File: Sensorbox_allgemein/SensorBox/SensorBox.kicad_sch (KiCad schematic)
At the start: 29 parts, among them J1 SD_Card, Q1 NPN, U2 PS1-O3-100, U3 Beetle ESP32-C6, U5 HPP845E131R5, U6 TPS629211QDRLRQ1

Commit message: code
änderung
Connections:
- net 1.8+: no longer C1.1, C2.1, HM2.2 (CSB), HM2.6 (VDDIO), HM2.8 (VDD)
- net VDD_3V3: now also C1.1, C2.1, HM2.2 (CSB), HM2.6 (VDDIO), HM2.8 (VDD)

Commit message: dee
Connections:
- net 1.8+ is gone; now on net VDD_3V3: R1.2, R2.2
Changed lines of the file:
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@@
+	(wire
+		(pts
+			(xy 157.48 116.84) (xy 158.75 116.84)
+		)
+		(stroke
+			(width 0)
+			(type default)
+		)
+	)
 	(wire
 		(pts
@@
 		(pts
 			(xy 219.71 114.3) (xy 255.27 114.3)
+		)
+		(stroke
+			(width 0)
+			(type default)
+		)
+	)
+	(wire
+		(pts
+			(xy 175.26 116.84) (xy 176.53 116.84)
 		)
 		(stroke
@@
 		)
 	)
-	(global_label "1.8+"
-		(shape input)
-		(at 157.48 116.84 0)
-		(fields_autoplaced yes)
-		(effects
-			(font
-				(size 1.27 1.27)
-			)
-			(justify left)
-		)
-		(property "Intersheetrefs" "${INTERSHEET_REFS}"
-			(at 165.0614 116.84 0)
-			(effects
-				(font
-					(size 1.27 1.27)
-				)
-				(justify left)
-				(hide yes)
-			)
-		)
-	)
 	(global_label "SCL_GPIO20"
 		(shape input)
@@
 		)
 	)
-	(global_label "1.8+"
-		(shape input)
-		(at 175.26 116.84 0)
-		(fields_autoplaced yes)
-		(effects
-			(font
-				(size 1.27 1.27)
-			)
-			(justify left)
-		)
-		(property "Intersheetrefs" "${INTERSHEET_REFS}"
-			(at 182.8414 116.84 0)
+	(global_label "VDD_3V3"
+		(shape input)
+		(at 158.75 116.84 0)
+		(fields_autoplaced yes)
+		(effects
+			(font
+				(size 1.27 1.27)
+			)
+			(justify left)
+		)
+		(property "Intersheetrefs" "${INTERSHEET_REFS}"
+			(at 169.839 116.84 0)
 			(effects
 				(font
@@
 				(hide yes)
 			)
+		)
+	)
+	(global_label "VDD_3V3"
+		(shape input)
+		(at 176.53 116.84 0)
+		(fields_autoplaced yes)
+		(effects
+			(font
+				(size 1.27 1.27)
+			)
+			(justify left)
+		)
+		(property "Intersheetrefs" "${INTERSHEET_REFS}"
+			(at 187.619 116.84 0)
+			(effects
+				(font
+					(size 1.27 1.27)
+				)
+				(justify left)
+				(hide yes)
+			)

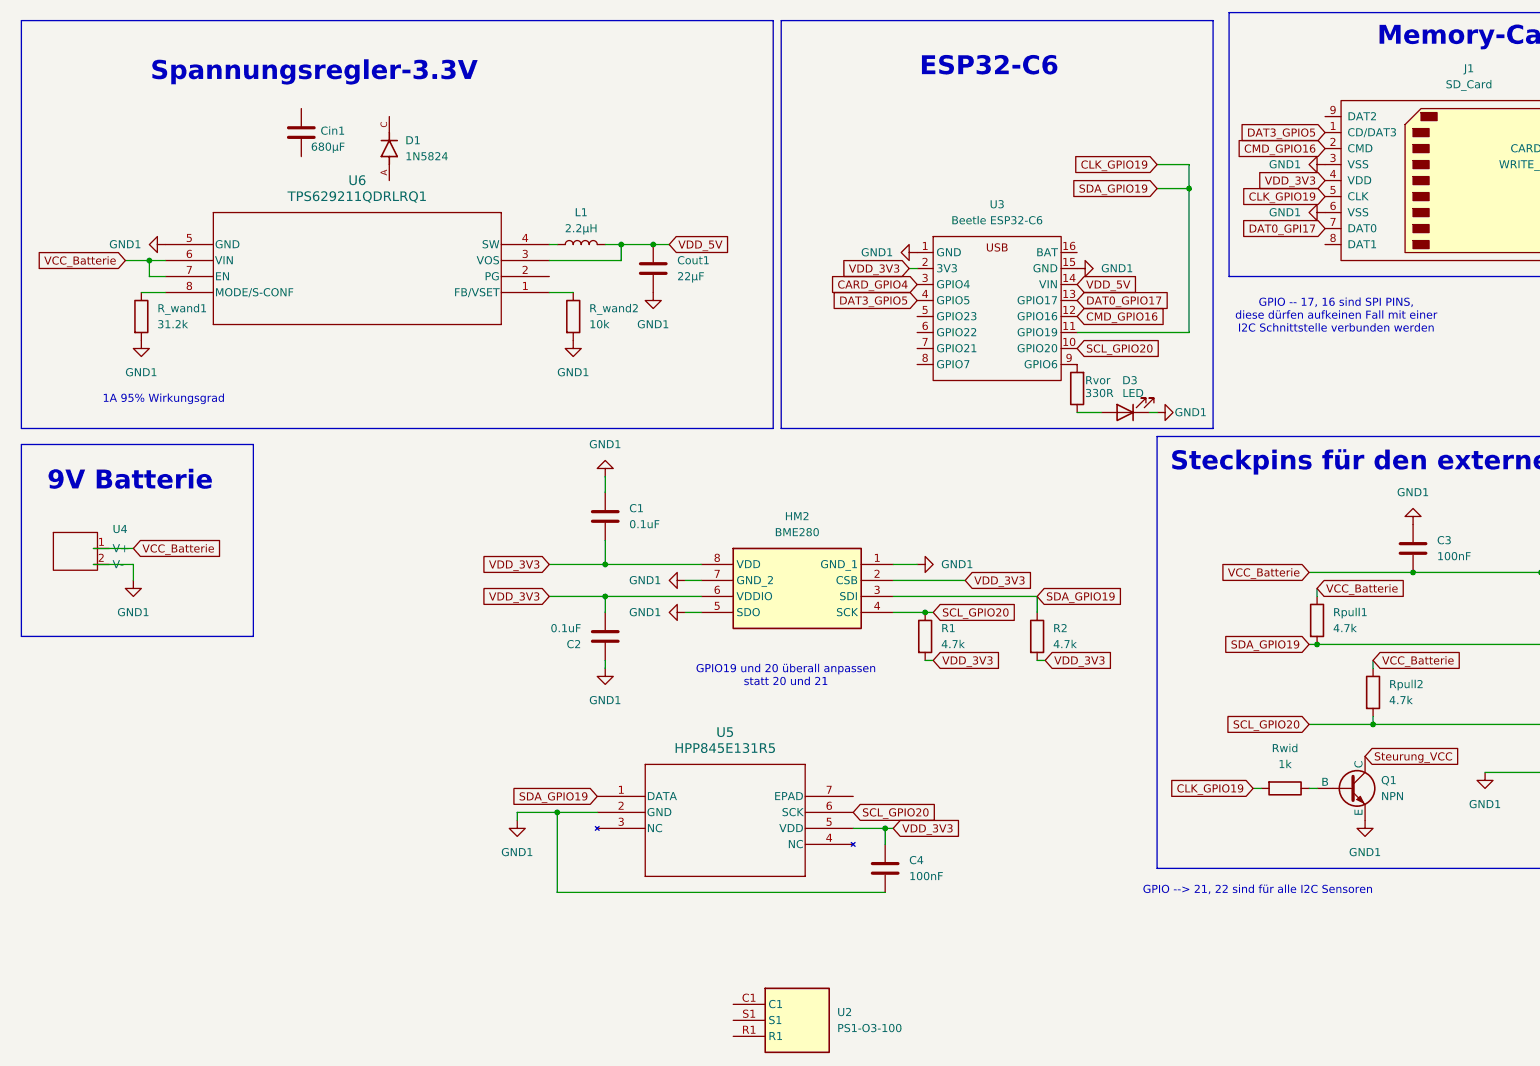
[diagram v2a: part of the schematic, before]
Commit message: Schaltplan
Schematic changed, fixes to hpp sensor and to the convertor. In addition changes to voltage supply
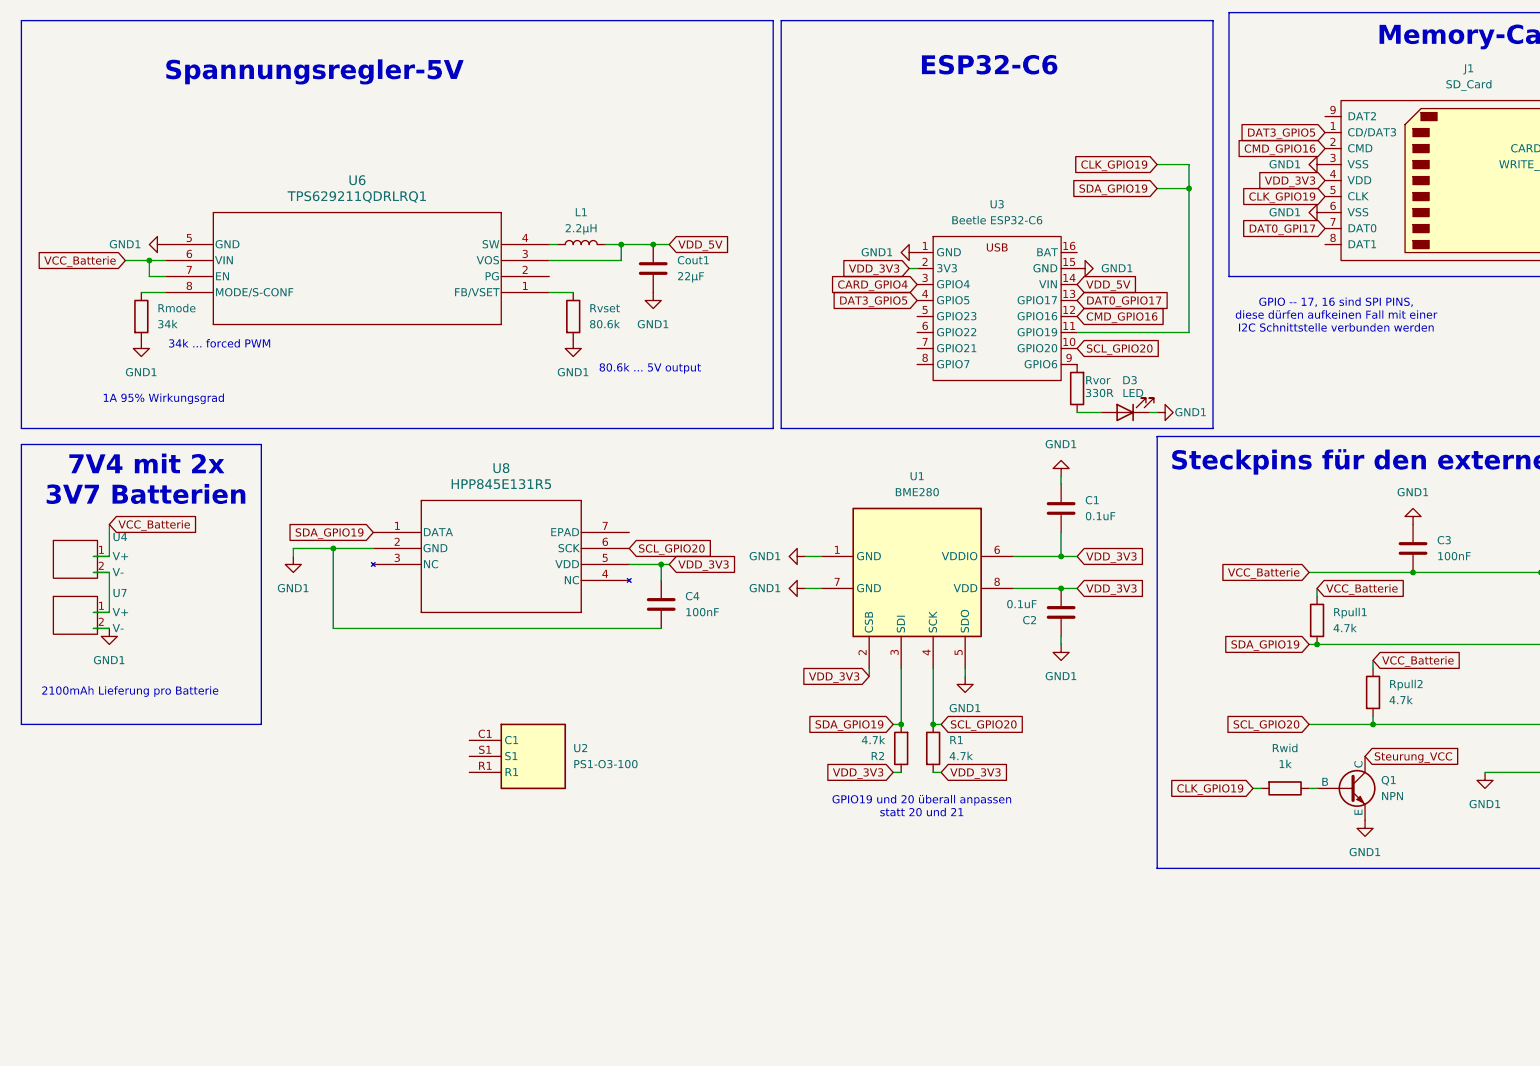
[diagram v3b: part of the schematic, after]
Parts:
- removed Cin1: 680µF, Capacitor_SMD:C_0402_1005Metric_Pad0.74x0.62mm_HandSolder, symbol Device:C
- removed D1: 1N5824, 1N5824:DIOAD1898W129L762D1143, symbol 1N5824:1N5824
- removed HM2: BME280, BME280_foot:BME280, symbol BME280_sym:BME280
- removed U5: HPP845E131R5, SON6_HPP845E131R5_TEC, symbol HPP845E131R5:HPP845E131R5
- added U1: BME280, Package_LGA:Bosch_LGA-8_2.5x2.5mm_P0.65mm_ClockwisePinNumbering, symbol Sensor:BME280
- added U7: ~, Battery_6V:Bat_3V7, symbol 6V_Battery_SensorBox:Battery_6V
- added U8: HPP845E131R5, HPP845E131R5:SON6_HPP845E131R5_TEC, symbol HPP845E131R5:HPP845E131R5
- Rmode: renamed from R_wand1; value 31.2k -> 34k
- Rvset: renamed from R_wand2; value 10k -> 80.6k
- U4: footprint Battery_6V:Bat_6V -> Battery_6V:Bat_3V7
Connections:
- net CLK_GPIO19: now also R2.2, U1.3 (SDI), U8.1 (DATA); no longer R2.1
- net GND1: now also U1.1 (GND), U1.5 (SDO), U1.7 (GND), U7.2 (V-), U8.2 (GND); no longer U4.2 (V-)
- net SCL_GPIO20: now also U1.4 (SCK), U8.6 (SCK)
- net VDD_3V3: now also R2.1, U1.2 (CSB), U1.6 (VDDIO), U1.8 (VDD), U8.5 (VDD); no longer R2.2
- new net: U4.2 (V-), U7.1 (V+)
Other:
- note added: "2100mAh Lieferung pro Batterie"
- note added: "34k ... forced PWM"
- note added: "7V4 mit 2x 3V7 Batterien"
- note added: "80.6k ... 5V output"
- note added: "Spannungsregler-5V"
- note removed: "9V Batterie"
- note removed: "GPIO --> 21, 22 sind für alle I2C Sensoren"
- note removed: "Spannungsregler-3.3V"
- moved on the sheet: C4, U2, U4

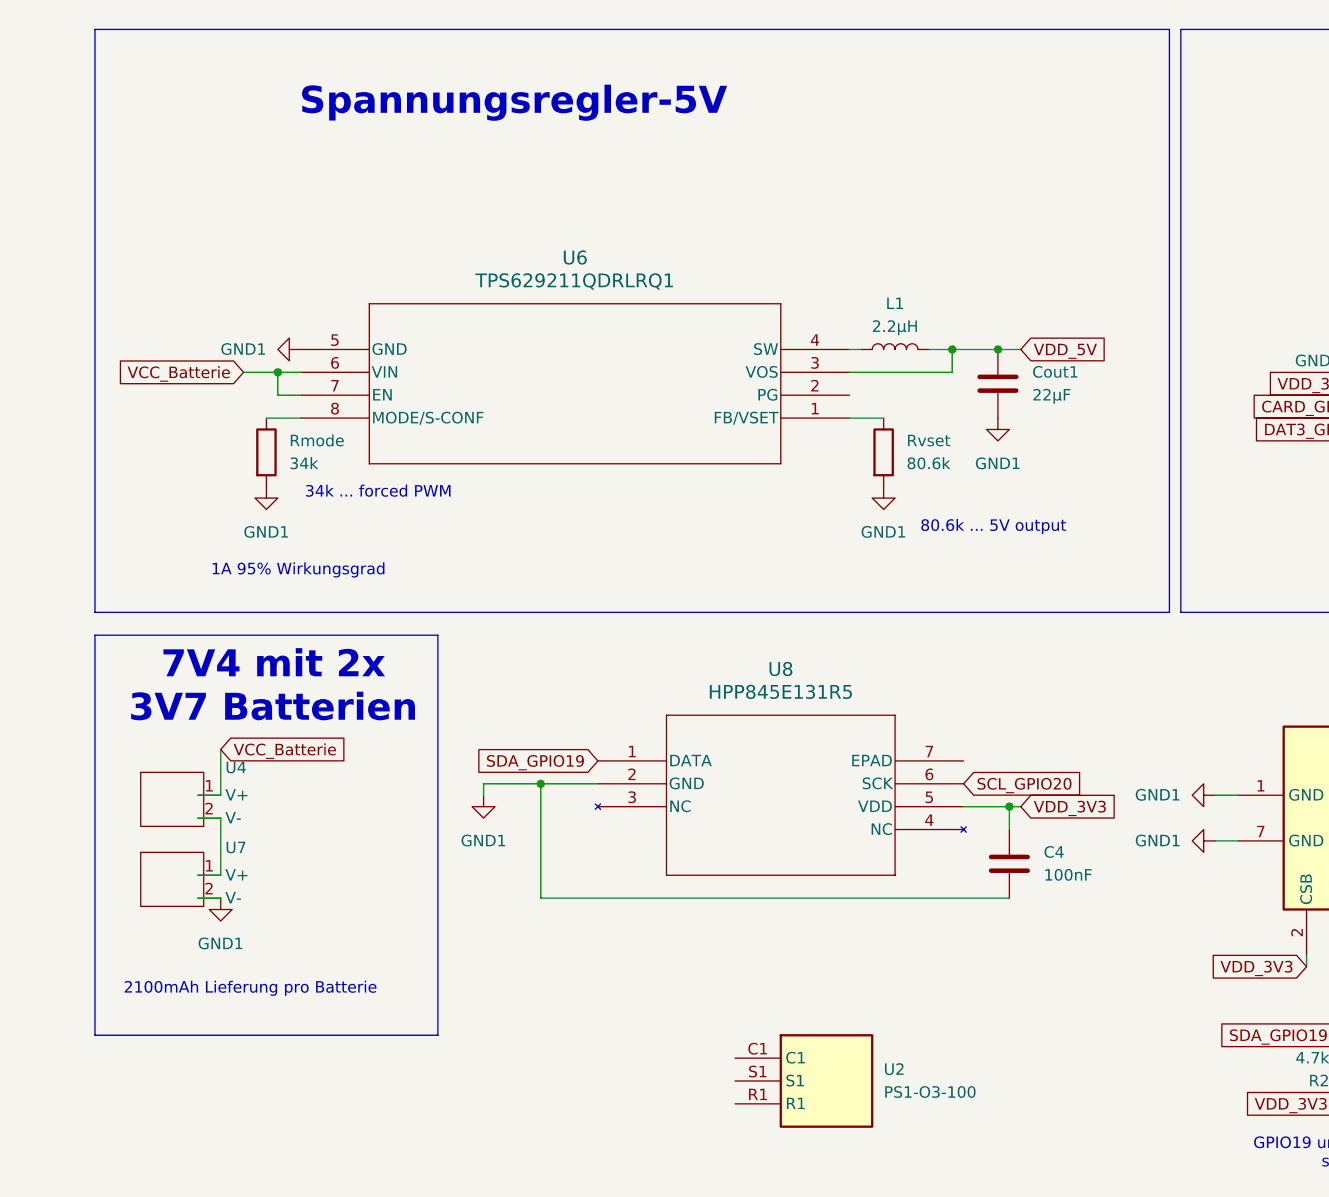
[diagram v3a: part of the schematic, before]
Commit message: Batterie und Regler
eingestellt und berechnet

Co-Authored-By: LinusMarte <174097811+LinusMarte@users.noreply.github.com>
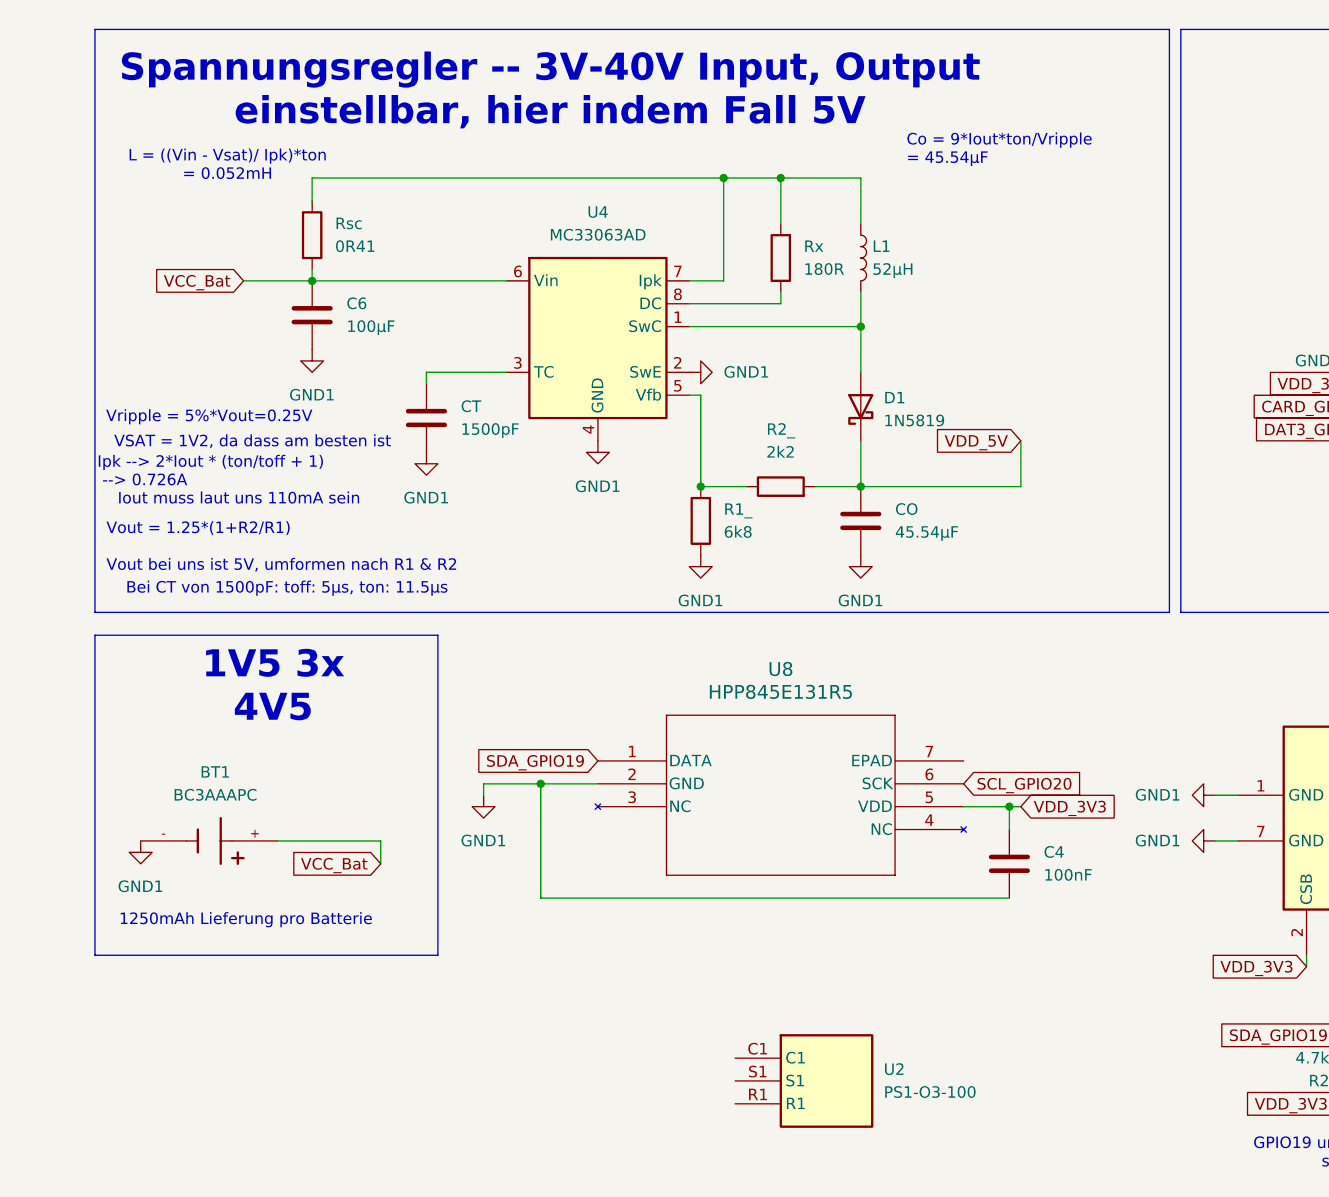
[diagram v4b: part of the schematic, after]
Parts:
- removed Cout1: 22µF, Capacitor_SMD:C_0402_1005Metric_Pad0.74x0.62mm_HandSolder, symbol Device:C
- removed Rmode: 34k, Resistor_SMD:R_0402_1005Metric, symbol Device:R
- removed Rvset: 80.6k, Resistor_SMD:R_0402_1005Metric, symbol Device:R
- removed U4, U7: ~, Battery_6V:Bat_3V7, symbol 6V_Battery_SensorBox:Battery_6V
- removed U6: TPS629211QDRLRQ1, footprints:SOT5X3_DRL_TEX, symbol 2024-11-18_14-00-38:TPS629211QDRLRQ1
- added BT1: BC3AAAPC, Battery:BatteryHolder_Keystone_2479_3xAAA, symbol BC3AAPC:BC3AAPC
- added C6: 100µF, Capacitor_SMD:C_0402_1005Metric_Pad0.74x0.62mm_HandSolder, symbol Device:C
- added CO: 45.54µF, Capacitor_SMD:C_0402_1005Metric_Pad0.74x0.62mm_HandSolder, symbol Device:C
- added CT: 1500pF, Capacitor_SMD:C_0402_1005Metric_Pad0.74x0.62mm_HandSolder, symbol Device:C
- added D1: 1N5819, Diode_THT:D_DO-41_SOD81_P10.16mm_Horizontal, symbol Diode:1N5819
- added R1_: 6k8, Resistor_SMD:R_0402_1005Metric, symbol Device:R
- added R2_: 2k2, Resistor_SMD:R_0402_1005Metric, symbol Device:R
- added Rsc: 0R41, Resistor_SMD:R_0402_1005Metric, symbol Device:R
- added Rx: 180R, Resistor_SMD:R_0402_1005Metric, symbol Device:R
- added U4: MC33063AD, Package_SO:SOIC-8_3.9x4.9mm_P1.27mm, symbol Regulator_Switching:MC33063AD
- L1: value 2.2µH -> 52µH
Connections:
- net GND1: now also BT1.-, C6.2, CO.2, CT.2, R1_.1, U4.2 (SwE), U4.4 (GND)
- net VDD_5V: now also CO.1, D1.1 (K), R2_.2; no longer L1.2
- net at L1.1: now also Rsc.1, Rx.2, U4.7 (Ipk)
- new net: R1_.2, R2_.1, U4.5 (Vfb)
- new net: CT.1, U4.3 (TC)
- new net: D1.2 (A), L1.2, U4.1 (SwC)
- new net: Rx.1, U4.8 (DC)
- new net VCC_Bat: BT1.+, C6.1, Rsc.2, U4.6 (Vin)
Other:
- note added: "1250mAh Lieferung pro Batterie"
- note added: "1V5 3x 4V5"
- note added: "Bei CT von 1500pF: toff: 5µs, ton: 11.5µs"
- note added: "Co = 9*Iout*ton/Vripple = 45.54µF"
- note added: "Iout muss laut uns 110mA sein"
- note added: "Ipk --> 2*Iout * (ton/toff + 1) --> 0.726A"
- note added: "L = ((Vin - Vsat)/ Ipk)*ton = 0.052mH"
- note added: "Spannungsregler -- 3V-40V Input, Output einstellbar, hier indem Fall 5V"
- note added: "VSAT = 1V2, da dass am besten ist"
- note added: "Vout = 1.25*(1+R2/R1) Vout bei uns ist 5V, umformen nach R1 & R2"
- note added: "Vripple = 5%*Vout=0.25V"
- note removed: "1A 95% Wirkungsgrad"
- note removed: "2100mAh Lieferung pro Batterie"
- note removed: "34k ... forced PWM"
- note removed: "7V4 mit 2x 3V7 Batterien"
- note removed: "80.6k ... 5V output"
- note removed: "Spannungsregler-5V"

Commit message: V3-Sensorbox
Externer sensor Type K geändert und Fuse/Sicherheitsschalter eingefügt
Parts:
- added C5: 0.1µF, Capacitor_SMD:C_0402_1005Metric_Pad0.74x0.62mm_HandSolder, symbol Device:C
- added F1: Fuse, Fuse:Fuseholder_TR5_Littelfuse_No560_No460, symbol Device:Fuse
- added TH2: Type K, Resistor_THT:R_Axial_DIN0204_L3.6mm_D1.6mm_P5.08mm_Horizontal, symbol Sensor_Temperature:PT100
- added U6: MAX31855EASA, Package_SO:SOIC-8_3.9x4.9mm_P1.27mm, symbol Sensor_Temperature:MAX31855EASA
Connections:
- net GND1: now also C5.2, U6.1 (GND)
- net VDD_3V3: now also C5.1, U6.4 (V_CC)
- net SCK_GPIO23: now reaches U3.5 (GPIO23)
- net SCK_GPIO23: now also U6.5 (SCK)
- net CS_GPIO22: now reaches U3.6 (GPIO22)
- net CS_GPIO22: now also U6.6 (~{CS})
- net Miso_GPIO21: now reaches U3.7 (GPIO21)
- net Miso_GPIO21: now also U6.7 (SO)
- new net: TH2.1, U6.2 (T-)
- new net: TH2.2, U6.3 (T+)
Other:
- note added: "Der MAX31855 wandelt die Spannung eines K-Typ Thermoelements in digitale Temperaturdaten um. Pin für den CS muss im Code beachtet werden!!"
- note added: "Type K Sensor (externer Sensor)"
- moved on the sheet: C3, GND1, Q1, Rpull1, Rpull2, Rwid, SCL, SDA/Signal, U2, VCC

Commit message: änderungen
50h gecheckt, bme angepasst

bme und hpp beschriftet

Eingang und Ausgang leitungen angepasst nach draußen oder nach innen
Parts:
- removed C3: 100nF, Capacitor_SMD:C_0402_1005Metric_Pad0.74x0.62mm_HandSolder, symbol Device:C
- removed D3: LED, LED_SMD:LED_0402_1005Metric, symbol Device:LED
- removed GND1, SCL, SDA/Signal, VCC: Conn_01x01_Socket, Connector_PinHeader_2.00mm:PinHeader_1x01_P2.00mm_Vertical, symbol Connector:Conn_01x01_Socket
- removed Q1: NPN, symbol Simulation_SPICE:NPN
- removed R2, Rpull1, Rpull2: 4.7k, Resistor_SMD:R_0402_1005Metric, symbol Device:R
- removed Rvor: 330R, Resistor_SMD:R_0402_1005Metric, symbol Device:R
- removed Rwid: 1k, Resistor_SMD:R_0402_1005Metric, symbol Device:R
- added D2: 1N5819, Diode_THT:D_DO-41_SOD81_P10.16mm_Horizontal, symbol Diode:1N5819
- added SW1: SW_SPST, Button_Switch_THT:SW_SPST_Omron_B3F-40xx, symbol Switch:SW_SPST
- R1: value 4.7k -> 10k
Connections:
- net CLK_GPIO19: no longer U1.3 (SDI), U3.11 (GPIO19), U8.1 (DATA)
- net GND1: now also C1.1, C2.1, R1.2; no longer C1.2, C2.2, U1.5 (SDO)
- net SCL_GPIO20: no longer R1.1
- net VCC_Bat: now also SW1.2 (B); no longer BT1.+
- net VDD_3V3: now also C1.2, C2.2, D2.1 (K); no longer C1.1, C2.1, R1.2
- net at F1.1: now also BT1.+
- net at F1.2: now also SW1.1 (A)
- new net: D2.2 (A), R1.1, U1.5 (SDO)
- new net SDA_GPIO19: U1.3 (SDI), U3.11 (GPIO19), U8.1 (DATA)
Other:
- note added: "BME280-Sensor"
- note added: "Dauer --> P_BAT / P_Verbrauch = 46.06h"
- note added: "HPP845E131R5-Sensor"
- note added: "P_BAT = 5.625Wh"
- note added: "P_Verbrauch = 0.122Wh"
- note added: "Schutz für Überspannung"
- note removed: "GPIO19 und 20 überall anpassen statt 20 und 21"
- note removed: "Steckpins für den externen Sensor"
- moved on the sheet: BT1, C4, F1, U1, U2, U8
